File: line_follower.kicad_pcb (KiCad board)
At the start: 2 copper layers, 93 parts, among them J1 Conn_01x20_Socket, J10 Conn_01x20_Pin, J11 Conn_01x20_Pin, J12 Conn_01x02_Socket, J2 Conn_01x20_Socket, J3 Conn_01x06_Socket, J4 Conn_01x06_Socket, J5 XT60-M, J6 Conn_01x02_Socket, J7 Conn_01x02_Socket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

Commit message: some placement done
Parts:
- A1, A2, A3, A4, A5, A6, A7, A8, A9: moved to B.Cu
- moved C2 183.6 mm to (273.9, 85.6)
- moved D1 183.6 mm to (299.1, 121.0)
- moved D11 183.6 mm to (307.9, 121.0)
- moved D12 183.6 mm to (307.9, 123.6)
- moved D13 183.6 mm to (307.9, 126.2)
- moved D14 183.6 mm to (307.9, 128.8)
- moved F1 183.6 mm to (287.5, 139.1)
- moved J3 183.6 mm to (285.4, 111.8)
- moved J4 183.6 mm to (290.0, 111.8)
- moved J6 183.6 mm to (297.0, 103.5)
- moved J7 183.6 mm to (301.6, 103.5)
- moved J9 183.6 mm to (306.2, 103.5)
- moved R1 183.6 mm to (278.5, 108.2)
- moved SW1 183.6 mm to (274.9, 112.0)
- moved SW3 183.6 mm to (274.9, 122.9)
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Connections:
- R11 pad 2: /CALIB -> /PA1
- R12 pad 2: /PA1 -> /PA2
- R13 pad 2: /PA2 -> /PA3
- R14 pad 2: /PA3 -> /PA4
- R15 pad 2: /PA4 -> /PA5
- R16 pad 2: /PA5 -> /PA6
- R17 pad 2: /PA6 -> /PA7
- R18 pad 2: /PA7 -> /PB0
- R19 pad 2: /PB0 -> /PB1
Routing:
- net GND: track 0.00 -> 20.3 mm
- net /5V_STM: track 0.00 -> 20.3 mm
- net /3.3V_STM: track 0.00 -> 20.3 mm
- net /VBAT_STM: track 0.00 -> 10.2 mm
- net /PC15: track 0.00 -> 10.2 mm
- net /PC13: track 0.00 -> 10.2 mm
- net /PB9: track 0.00 -> 10.2 mm
- net /PB7: track 0.00 -> 10.2 mm
- net /PB6: track 0.00 -> 10.2 mm
- net /PB5: track 0.00 -> 10.2 mm
- net /PB4: track 0.00 -> 10.2 mm
- net /PB3: track 0.00 -> 10.2 mm
- net /PB2: track 0.00 -> 10.2 mm
- net /PB14: track 0.00 -> 10.2 mm
- net /PB13: track 0.00 -> 10.2 mm
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
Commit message: placement done
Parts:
- moved J12 230.1 mm to (98.3, 192.0), turned to 90 degrees
- moved J9 229.2 mm to (88.2, 174.2), turned to 90 degrees
- moved J6 226.8 mm to (88.2, 192.0), turned to 90 degrees
- moved D1 222.5 mm to (90.7, 198.9), turned to 90 degrees
- moved J7 215.2 mm to (98.3, 174.2), turned to 90 degrees
- moved R1 212.0 mm to (86.9, 198.9), turned to 90 degrees
- moved F1 209.9 mm to (89.7, 209.0), turned to 90 degrees
- moved SW1 198.9 mm to (96.9, 200.5)
- moved J3 197.5 mm to (125.5, 227.6), turned to 90 degrees
- moved C2 193.8 mm to (131.9, 217.4)
- moved J4 192.8 mm to (125.5, 212.3), turned to 90 degrees
- moved SW4 183.5 mm to (111.6, 217.4)
- moved R32 171.6 mm to (162.3, 215.1)
- moved R31 166.9 mm to (165.9, 209.6)
- moved R29 166.7 mm to (165.9, 204.2)
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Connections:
- D10 pad 1: Net-(D10-K) -> GND
- D10 pad 2: /PB2 -> Net-(D10-A)
- D11 pad 1: Net-(D11-K) -> GND
- D11 pad 2: /PB9 -> Net-(D11-A)
- D12 pad 1: Net-(D12-K) -> GND
- D12 pad 2: /LEFT -> Net-(D12-A)
- D13 pad 1: Net-(D13-K) -> GND
- D13 pad 2: /PC13 -> Net-(D13-A)
- D14 pad 1: Net-(D14-K) -> GND
- D14 pad 2: /CALIB -> Net-(D14-A)
- D2 pad 1: Net-(D2-K) -> GND
- D2 pad 2: /PB12 -> Net-(D2-A)
- D3 pad 1: Net-(D3-K) -> GND
- D3 pad 2: /PB13 -> Net-(D3-A)
- D4 pad 1: Net-(D4-K) -> GND
- D4 pad 2: /PB14 -> Net-(D4-A)
- D5 pad 1: Net-(D5-K) -> GND
- D5 pad 2: /PA12 -> Net-(D5-A)
- D6 pad 1: Net-(D6-K) -> GND
- D6 pad 2: /PA15 -> Net-(D6-A)
- D7 pad 1: Net-(D7-K) -> GND
- D7 pad 2: /PB3 -> Net-(D7-A)
- D8 pad 1: Net-(D8-K) -> GND
- D8 pad 2: /PB4 -> Net-(D8-A)
- D9 pad 1: Net-(D9-K) -> GND
- D9 pad 2: /PB10 -> Net-(D9-A)
- J4 pad 1: /IN4 -> /IN1
- J4 pad 2: /IN3 -> /IN2
- J4 pad 5: /IN2 -> /IN3
- J4 pad 6: /IN1 -> /IN4
- J5 pad 1: (no net) -> GND
- J5 pad 2: (no net) -> BAT+
- R20 pad 1: Net-(D2-K) -> Net-(D2-A)
- R20 pad 2: GND -> /PB12
- R21 pad 1: Net-(D3-K) -> Net-(D3-A)
- R21 pad 2: GND -> /PB13
- R22 pad 1: Net-(D4-K) -> Net-(D4-A)
- R22 pad 2: GND -> /PB14
- R23 pad 1: Net-(D5-K) -> Net-(D5-A)
- R23 pad 2: GND -> /PA12
- R24 pad 1: Net-(D6-K) -> Net-(D6-A)
- R24 pad 2: GND -> /PA15
- R25 pad 1: Net-(D7-K) -> Net-(D7-A)
- R25 pad 2: GND -> /PB3
- R26 pad 1: Net-(D8-K) -> Net-(D8-A)
- R26 pad 2: GND -> /PB4
- R27 pad 1: Net-(D9-K) -> Net-(D9-A)
- R27 pad 2: GND -> /PB10
- R28 pad 1: Net-(D10-K) -> Net-(D10-A)
- R28 pad 2: GND -> /PB2
- R29 pad 1: Net-(D11-K) -> /PB9
- R29 pad 2: GND -> Net-(D11-A)
- R30 pad 1: Net-(D12-K) -> /LEFT
- R30 pad 2: GND -> Net-(D12-A)
- R31 pad 1: Net-(D13-K) -> /PC13
- R31 pad 2: GND -> Net-(D13-A)
- R32 pad 1: Net-(D14-K) -> /CALIB
- R32 pad 2: GND -> Net-(D14-A)
- SW1 pad 4: (no net) -> /FUSE_OUT 
- SW1 pad 5: (no net) -> /BUCK_IN
- SW3 pad 4: (no net) -> /CALIB
- SW3 pad 5: (no net) -> /3.3V_STM
- SW4 pad 4: (no net) -> /BUCK_IN
- SW4 pad 5: (no net) -> /VCC_DRV
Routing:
- net /BUCK_IN: track 0.00 -> 24.9 mm
- net GND: track 20.3 -> 31.6 mm
- net /FUSE_OUT : track 0.00 -> 7.65 mm
- net BAT+: track 0.00 -> 4.08 mm
- net /PC15: track 10.2 -> 14.1 mm
- net /pow_led-: track 0.00 -> 3.82 mm
- net /CALIB: track 10.2 -> 13.6 mm
- net /PB9: track 10.2 -> 7.62 mm
- net /PB7: track 10.2 -> 7.62 mm
- net /PB6: track 10.2 -> 7.62 mm
- net /PB5: track 10.2 -> 7.62 mm
- net /PB4: track 10.2 -> 7.62 mm
- net /PB3: track 10.2 -> 7.62 mm
- net /PB14: track 10.2 -> 7.62 mm
- net /PB13: track 10.2 -> 7.62 mm
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- added copper zone on F.Cu, net /FUSE_OUT 
- added copper zone on F.Cu, net BAT+
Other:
- board outline added: 151.1 x 167.8 mm
- board text added: "CALIBRATION"
- board text added: "LEFT"
- board text added: "RIGHT"
- board text added: "STRAIGHT"

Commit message: minor design errors left
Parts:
- added 1: MountingHole_2.1mm, MountingHole:MountingHole_2.1mm, F.Cu at (70.9, 181.0)
- added 2: MountingHole_2.1mm, MountingHole:MountingHole_2.1mm, F.Cu at (70.9, 208.0)
- added 3: MountingHole_2.1mm, MountingHole:MountingHole_2.1mm, F.Cu at (203.0, 181.0)
- added 4: MountingHole_2.1mm, MountingHole:MountingHole_2.1mm, F.Cu at (203.0, 208.0)
- added C22: 22uf, Capacitor_SMD:C_0603_1608Metric_Pad1.08x0.95mm_HandSolder, F.Cu at (89.7, 183.9)
- added C23: 22uf, Capacitor_SMD:C_0603_1608Metric_Pad1.08x0.95mm_HandSolder, F.Cu at (102.6, 188.5)
- added J13: Conn_01x04_Pin, Connector_PinHeader_2.54mm:PinHeader_1x04_P2.54mm_Vertical, F.Cu at (129.3, 237.5)
- added U1: AMS1117-3.3, Package_TO_SOT_SMD:SOT-223-3_TabPin2, F.Cu at (96.0, 186.4)
- R10, R2, R3, R4, R5, R6, R7, R8, R9: moved to B.Cu
- moved R2 94.7 mm to (89.9, 93.2), turned to 180 degrees
- moved R10 92.4 mm to (182.4, 93.7)
- moved D5 77.8 mm to (142.2, 159.5)
- moved D9 77.6 mm to (131.1, 159.5)
- moved D10 77.5 mm to (136.7, 159.0)
- moved D4 77.3 mm to (125.5, 160.0)
- moved D6 76.8 mm to (147.8, 160.0)
- moved D3 75.7 mm to (119.9, 160.5)
- moved D7 75.2 mm to (153.4, 160.5)
- moved D8 73.2 mm to (159.0, 161.8), turned to -90 degrees
- moved D2 71.6 mm to (114.3, 161.5), turned to -90 degrees
- moved R3 70.8 mm to (103.1, 85.1), turned to -135 degrees
- moved R9 68.8 mm to (168.4, 85.1)
- moved R4 46.7 mm to (115.6, 80.8), turned to 45 degrees
- moved R8 46.3 mm to (157.2, 82.3)
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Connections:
- A1 pad 1: Net-(A1-Pad1) -> /RPR_ANO
- A2 pad 1: Net-(A2-Pad1) -> /RPR_ANO
- A3 pad 1: Net-(A3-Pad1) -> /RPR_ANO
- A4 pad 1: Net-(A4-Pad1) -> /RPR_ANO
- A5 pad 1: Net-(A5-Pad1) -> /RPR_ANO
- A6 pad 1: Net-(A6-Pad1) -> /RPR_ANO
- A7 pad 1: Net-(A7-Pad1) -> /RPR_ANO
- A8 pad 1: Net-(A8-Pad1) -> /RPR_ANO
- A9 pad 1: Net-(A9-Pad1) -> /RPR_ANO
- C10 pad 1: /3.3V_STM -> /RPR_ANO
- C11 pad 1: /3.3V_STM -> /RPR_ANO
- C12 pad 1: /3.3V_STM -> /RPR_ANO
- C3 pad 1: /3.3V_STM -> /RPR_ANO
- C5 pad 1: /3.3V_STM -> /RPR_ANO
- C6 pad 1: /3.3V_STM -> /RPR_ANO
- C7 pad 1: /3.3V_STM -> /RPR_ANO
- C8 pad 1: /3.3V_STM -> /RPR_ANO
- C9 pad 1: /3.3V_STM -> /RPR_ANO
- J1 pad 18: /LEFT -> /PC14
- J1 pad 19: /PC13 -> /LEFT
- J11 pad 18: /LEFT -> /PC14
- J11 pad 19: /PC13 -> /LEFT
- J3 pad 3: /OUT1 -> /OUT2
- J3 pad 4: /OUT1 -> /OUT3
- J3 pad 5: /OUT1 -> /OUT4
- R10 pad 2: Net-(A9-Pad1) -> /RPR_ANO
- R2 pad 2: Net-(A1-Pad1) -> /RPR_ANO
- R29 pad 1: /PB9 -> /PC14
- R3 pad 2: Net-(A2-Pad1) -> /RPR_ANO
- R31 pad 1: /PC13 -> /PC15
- R4 pad 2: Net-(A3-Pad1) -> /RPR_ANO
- R5 pad 2: Net-(A4-Pad1) -> /RPR_ANO
- R6 pad 2: Net-(A5-Pad1) -> /RPR_ANO
- R7 pad 2: Net-(A6-Pad1) -> /RPR_ANO
- R8 pad 2: Net-(A7-Pad1) -> /RPR_ANO
- R9 pad 2: Net-(A8-Pad1) -> /RPR_ANO
- SW5 pad 2: /PC15 -> /PB9
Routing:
- net /5V_STM: track 17.8 -> 528.0 mm, vias 0 -> 6
- net /3.3V_STM: track 21.2 -> 294.0 mm, vias 0 -> 2
- net /PA1: track 7.62 -> 153.0 mm, vias 0 -> 2
- net /PB1: track 7.62 -> 150.1 mm
- net /PA2: track 7.62 -> 141.0 mm, vias 0 -> 2
- net /PB0: track 7.62 -> 136.5 mm
- net /RPR_ANO: track 0.00 -> 128.0 mm
- net /PA3: track 7.62 -> 131.5 mm, vias 0 -> 2
- net /PA7: track 7.62 -> 124.2 mm
- net /PA4: track 7.62 -> 118.3 mm
- net /PA6: track 7.62 -> 114.4 mm
- net /PA5: track 7.62 -> 109.8 mm
- net GND: track 31.6 -> 123.1 mm, vias 0 -> 32
- net Net-(D5-A): track 0.00 -> 84.6 mm, vias 0 -> 2
- net Net-(D6-A): track 0.00 -> 75.7 mm, vias 0 -> 2
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- added copper zone on B.Cu, net GND
- added copper zone on F.Cu, net GND
- removed copper zone on F.Cu, net BAT+
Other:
- board size 151.1 x 167.8 mm -> 151.1 x 176.3 mm
- board text added: "MOTOR MOUNTS"

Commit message: pcb finished
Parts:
- R20, R21, R22, R23, R24, R25, R26, R27, R28, R29, R30, R31, R32: value 220 -> 150
- moved C15 12.0 mm to (166.0, 77.4)
- moved C16 11.4 mm to (153.5, 74.9)
- moved C19 11.4 mm to (117.3, 78.1)
- moved C18 11.4 mm to (129.9, 75.2)
- moved C17 11.4 mm to (141.6, 75.4)
- moved C14 10.7 mm to (177.4, 81.3)
- moved C13 10.7 mm to (186.6, 87.9)
- moved C20 10.3 mm to (105.2, 82.1), turned to 90 degrees
- moved R8 9.89 mm to (166.3, 78.3), turned to -135 degrees
- moved R9 9.81 mm to (177.7, 81.9), turned to -135 degrees
- moved R2 9.52 mm to (94.8, 85.0), turned to -90 degrees
- moved R10 8.87 mm to (187.5, 86.5), turned to 180 degrees
- moved R3 7.17 mm to (105.3, 78.3)
- moved R6 6.74 mm to (140.9, 72.7), turned to -135 degrees
- moved R7 6.47 mm to (153.5, 73.9), turned to 135 degrees
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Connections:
- A1 pad 3: GND -> /PA1
- A1 pad 4: /PA1 -> /3.3V_STM
- A2 pad 3: GND -> /PA2
- A2 pad 4: /PA2 -> /3.3V_STM
- A3 pad 3: GND -> /PA3
- A3 pad 4: /PA3 -> /3.3V_STM
- A4 pad 3: GND -> /PA4
- A4 pad 4: /PA4 -> /3.3V_STM
- A5 pad 3: GND -> /PA5
- A5 pad 4: /PA5 -> /3.3V_STM
- A6 pad 3: GND -> /PA6
- A6 pad 4: /PA6 -> /3.3V_STM
- A7 pad 3: GND -> /PA7
- A7 pad 4: /PA7 -> /3.3V_STM
- A8 pad 3: GND -> /PB0
- A8 pad 4: /PB0 -> /3.3V_STM
- A9 pad 3: GND -> /PB1
- A9 pad 4: /PB1 -> /3.3V_STM
- C13 pad 1: /5V_STM -> /3.3V_STM
- C14 pad 1: /5V_STM -> /3.3V_STM
- C15 pad 1: /5V_STM -> /3.3V_STM
- C16 pad 1: /5V_STM -> /3.3V_STM
- C17 pad 1: /5V_STM -> /3.3V_STM
- C18 pad 1: /5V_STM -> /3.3V_STM
- C19 pad 1: /5V_STM -> /3.3V_STM
- C20 pad 1: /5V_STM -> /3.3V_STM
- C21 pad 1: /5V_STM -> /3.3V_STM
- R10 pad 1: /3.3V_STM -> /5V_STM
- R11 pad 1: /5V_STM -> GND
- R12 pad 1: /5V_STM -> GND
- R13 pad 1: /5V_STM -> GND
- R14 pad 1: /5V_STM -> GND
- R15 pad 1: /5V_STM -> GND
- R16 pad 1: /5V_STM -> GND
- R17 pad 1: /5V_STM -> GND
- R18 pad 1: /5V_STM -> GND
- R19 pad 1: /5V_STM -> GND
- R2 pad 1: /3.3V_STM -> /5V_STM
- R3 pad 1: /3.3V_STM -> /5V_STM
- R4 pad 1: /3.3V_STM -> /5V_STM
- R5 pad 1: /3.3V_STM -> /5V_STM
- R6 pad 1: /3.3V_STM -> /5V_STM
- R7 pad 1: /3.3V_STM -> /5V_STM
- R8 pad 1: /3.3V_STM -> /5V_STM
- R9 pad 1: /3.3V_STM -> /5V_STM
- SW4 pad 1: /BUCK_IN -> BAT+
- SW4 pad 4: /BUCK_IN -> BAT+
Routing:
- net /3.3V_STM: track 294.0 -> 472.9 mm, vias 2 -> 3
- net /5V_STM: track 528.0 -> 415.1 mm, vias 6 -> 5
- net BAT+: track 12.9 -> 69.2 mm
- net /RPR_ANO: track 128.0 -> 91.7 mm
- net GND: track 123.1 -> 151.2 mm, vias 32 -> 220
- net /BUCK_IN: track 65.0 -> 40.7 mm
- net /PA1: track 153.0 -> 145.2 mm, vias 2 -> 0
- net /FUSE_OUT : track 7.65 -> 13.3 mm
- net /PA6: track 114.4 -> 119.9 mm
- net /PA3: track 131.5 -> 126.1 mm, vias 2 -> 0
- net /PA2: track 141.0 -> 136.1 mm, vias 2 -> 0
- net /PA7: track 124.2 -> 128.2 mm
- net /PB0: track 136.5 -> 139.1 mm
- net /PB1: track 150.1 -> 148.6 mm
- net /PA5: track 109.8 -> 111.0 mm
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- removed copper zone on F.Cu, net /FUSE_OUT 
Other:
- outline, holes or cut-outs redrawn

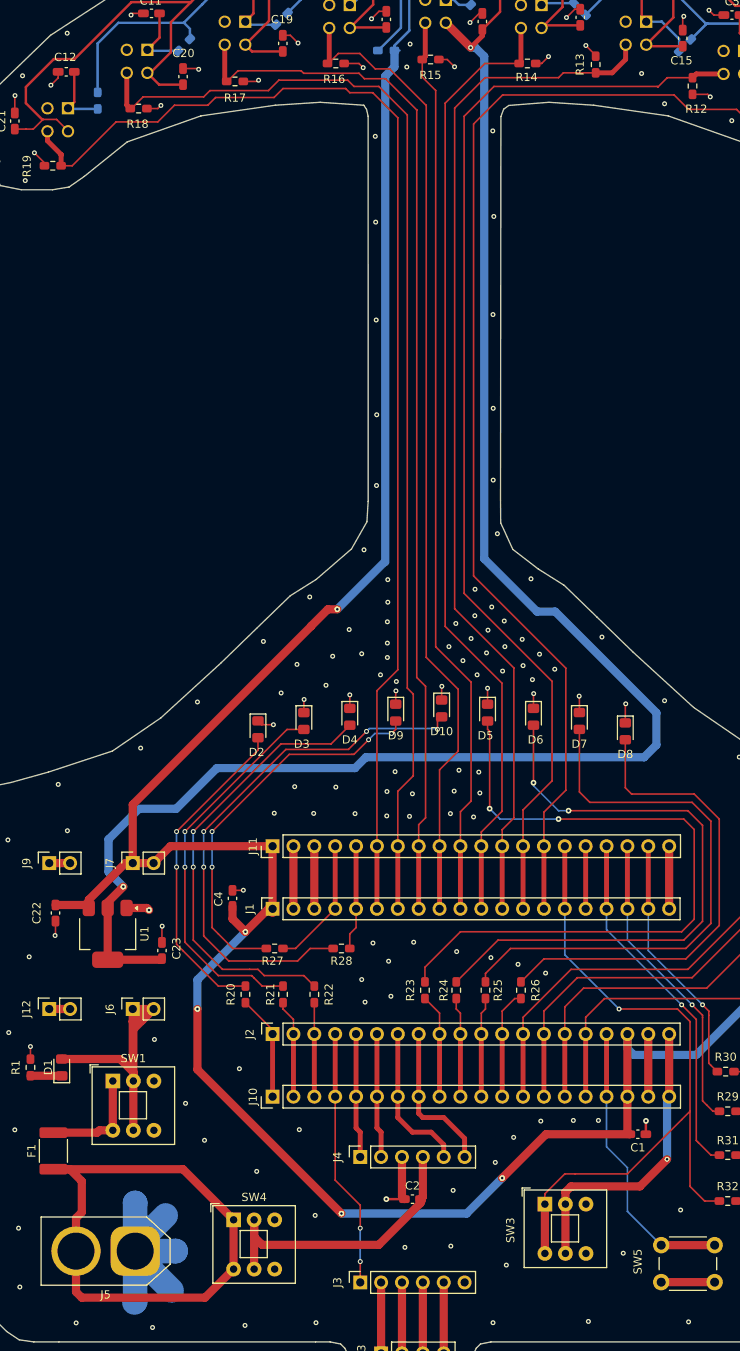
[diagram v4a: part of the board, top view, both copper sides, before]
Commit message: all drc errors fixed
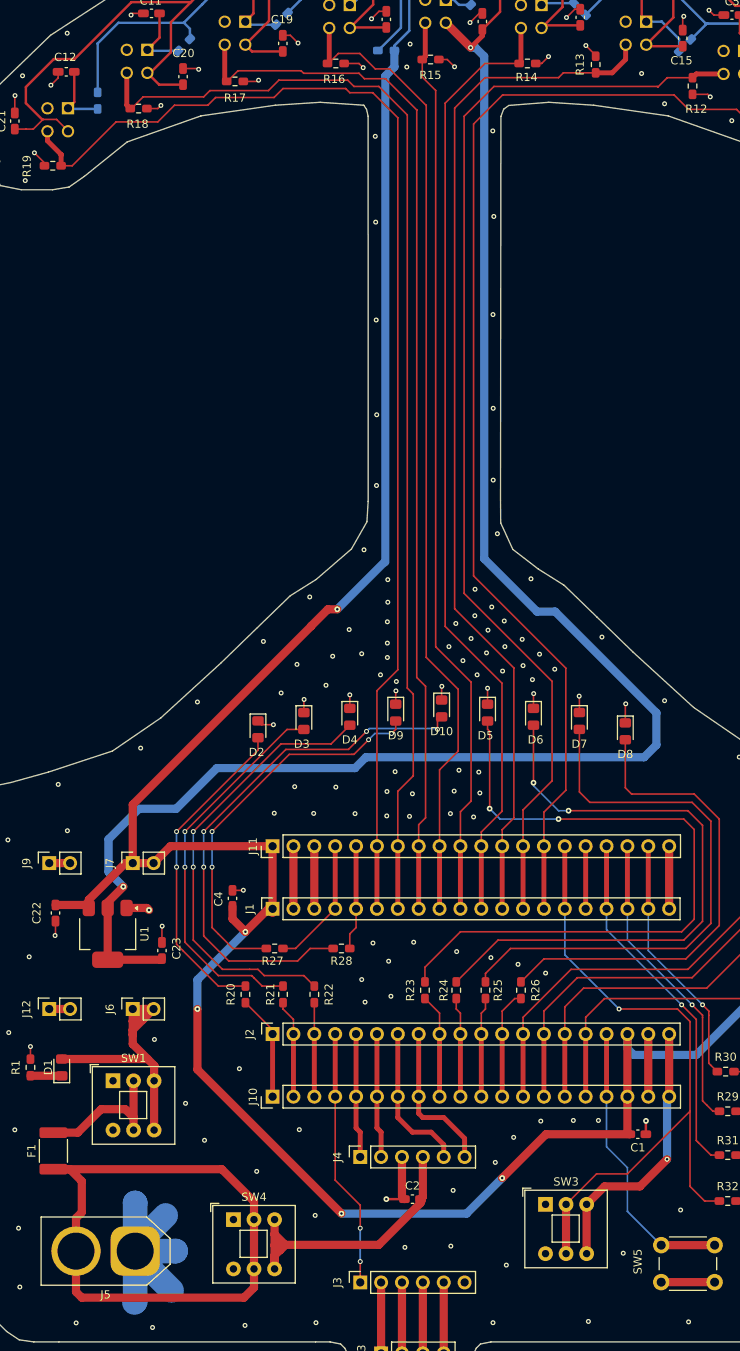
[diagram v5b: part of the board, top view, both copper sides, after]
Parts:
- SW1, SW3, SW4: value SW_Push -> SW_Push_DPDT
- moved SW3 0.08 mm to (149.3, 219.4)
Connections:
- A1 pad 1: /RPR_ANO -> /RPR_ANO_9
- A1 pad 4: /3.3V_STM -> /3.3V_LDO
- A2 pad 1: /RPR_ANO -> /RPR_ANO_8
- A2 pad 4: /3.3V_STM -> /3.3V_LDO
- A3 pad 1: /RPR_ANO -> /RPR_ANO_7
- A3 pad 4: /3.3V_STM -> /3.3V_LDO
- A4 pad 1: /RPR_ANO -> /RPR_ANO_6
- A4 pad 4: /3.3V_STM -> /3.3V_LDO
- A5 pad 1: /RPR_ANO -> /RPR_ANO_5
- A5 pad 4: /3.3V_STM -> /3.3V_LDO
- A6 pad 1: /RPR_ANO -> /RPR_ANO_4
- A6 pad 4: /3.3V_STM -> /3.3V_LDO
- A7 pad 1: /RPR_ANO -> /RPR_ANO_3
- A7 pad 4: /3.3V_STM -> /3.3V_LDO
- A8 pad 1: /RPR_ANO -> /RPR_ANO_2
- A8 pad 4: /3.3V_STM -> /3.3V_LDO
- A9 pad 1: /RPR_ANO -> /RPR_ANO_1
- A9 pad 4: /3.3V_STM -> /3.3V_LDO
- C10 pad 1: /RPR_ANO -> /RPR_ANO_3
- C11 pad 1: /RPR_ANO -> /RPR_ANO_2
- C12 pad 1: /RPR_ANO -> /RPR_ANO_1
- C13 pad 1: /3.3V_STM -> /3.3V_LDO
- C14 pad 1: /3.3V_STM -> /3.3V_LDO
- C15 pad 1: /3.3V_STM -> /3.3V_LDO
- C16 pad 1: /3.3V_STM -> /3.3V_LDO
- C17 pad 1: /3.3V_STM -> /3.3V_LDO
- C18 pad 1: /3.3V_STM -> /3.3V_LDO
- C19 pad 1: /3.3V_STM -> /3.3V_LDO
- C20 pad 1: /3.3V_STM -> /3.3V_LDO
- C21 pad 1: /3.3V_STM -> /3.3V_LDO
- C23 pad 1: /3.3V_STM -> /3.3V_LDO
- C3 pad 1: /RPR_ANO -> /RPR_ANO_9
- C5 pad 1: /RPR_ANO -> /RPR_ANO_8
- C6 pad 1: /RPR_ANO -> /RPR_ANO_7
- C7 pad 1: /RPR_ANO -> /RPR_ANO_6
- C8 pad 1: /RPR_ANO -> /RPR_ANO_5
- C9 pad 1: /RPR_ANO -> /RPR_ANO_4
- J10 pad 20: /3.3V_STM -> /3.3V_STM_1
- J2 pad 20: /3.3V_STM -> /3.3V_STM_1
- R10 pad 2: /RPR_ANO -> /RPR_ANO_9
- R2 pad 2: /RPR_ANO -> /RPR_ANO_1
- R3 pad 2: /RPR_ANO -> /RPR_ANO_2
- R4 pad 2: /RPR_ANO -> /RPR_ANO_3
- R5 pad 2: /RPR_ANO -> /RPR_ANO_4
- R6 pad 2: /RPR_ANO -> /RPR_ANO_5
- R7 pad 2: /RPR_ANO -> /RPR_ANO_6
- R8 pad 2: /RPR_ANO -> /RPR_ANO_7
- R9 pad 2: /RPR_ANO -> /RPR_ANO_8
- SW1 pad 1: /FUSE_OUT  -> unconnected-(SW1-A-Pad1)
- SW1 pad 2: /BUCK_IN -> /FUSE_OUT 
- SW1 pad 3: (no net) -> /BUCK_IN
- SW1 pad 4: /FUSE_OUT  -> unconnected-(SW1-A-Pad4)
- SW1 pad 5: /BUCK_IN -> /FUSE_OUT 
- SW1 pad 6: (no net) -> /BUCK_IN
- SW3 pad 1: /CALIB -> unconnected-(SW3-A-Pad1)
- SW3 pad 2: /3.3V_STM -> /CALIB
- SW3 pad 3: (no net) -> /3.3V_STM_1
- SW3 pad 4: /CALIB -> unconnected-(SW3-A-Pad4)
- SW3 pad 5: /3.3V_STM -> /CALIB
- SW3 pad 6: (no net) -> /3.3V_STM_1
- SW4 pad 1: BAT+ -> unconnected-(SW4-A-Pad1)
- SW4 pad 2: /VCC_DRV -> BAT+
- SW4 pad 3: (no net) -> /VCC_DRV
- SW4 pad 4: BAT+ -> unconnected-(SW4-A-Pad4)
- SW4 pad 5: /VCC_DRV -> BAT+
- SW4 pad 6: (no net) -> /VCC_DRV
- U1 pad 2: /3.3V_STM -> /3.3V_LDO
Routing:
- net /3.3V_STM: track 472.9 -> 7.62 mm, vias 3 -> 0
- net /3.3V_LDO: track 0.00 -> 428.5 mm, vias 0 -> 2
- net /RPR_ANO: track 91.7 -> 0.00 mm
- net /3.3V_STM_1: track 0.00 -> 33.4 mm, vias 0 -> 1
- net /RPR_ANO_4: track 0.00 -> 19.7 mm
- net /RPR_ANO_7: track 0.00 -> 10.9 mm
- net /RPR_ANO_8: track 0.00 -> 9.66 mm
- net /RPR_ANO_9: track 0.00 -> 9.09 mm
- net /RPR_ANO_2: track 0.00 -> 8.85 mm
- net /RPR_ANO_3: track 0.00 -> 8.60 mm
- net /RPR_ANO_6: track 0.00 -> 8.46 mm
- net /RPR_ANO_1: track 0.00 -> 8.39 mm
- net /RPR_ANO_5: track 0.00 -> 7.97 mm
- net BAT+: track 69.2 -> 76.8 mm
- net /FUSE_OUT : track 13.3 -> 17.4 mm
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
